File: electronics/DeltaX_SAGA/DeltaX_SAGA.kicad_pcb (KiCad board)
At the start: 4 copper layers, 50 x 50 mm, 73 parts, among them J1 USB_B_Micro, J10 M3_Encoder, J11 OUT-, J12 OUT+, J13 OUT-, J14 OUT+, J15 OUT-, J16 +, J17 -, J2 Programmer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

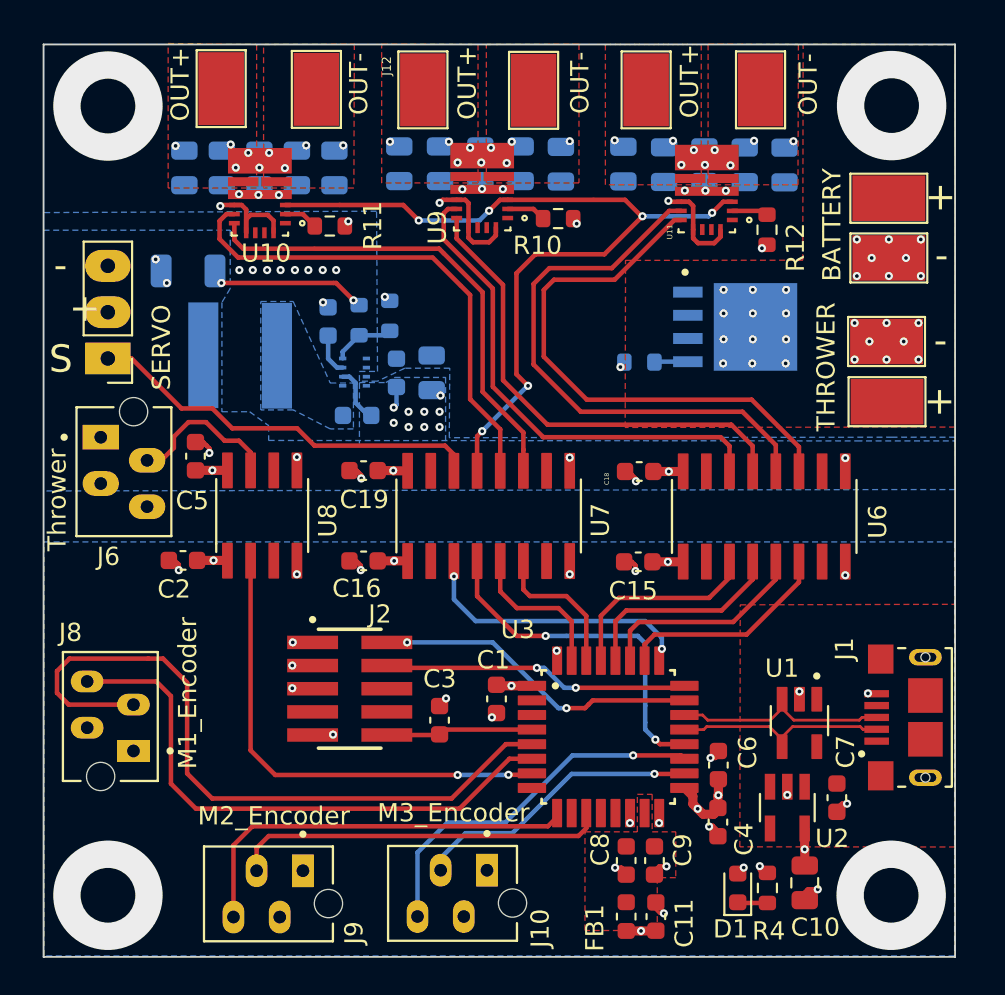
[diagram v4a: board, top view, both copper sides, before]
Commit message: PCB labels and routing optimised and updated
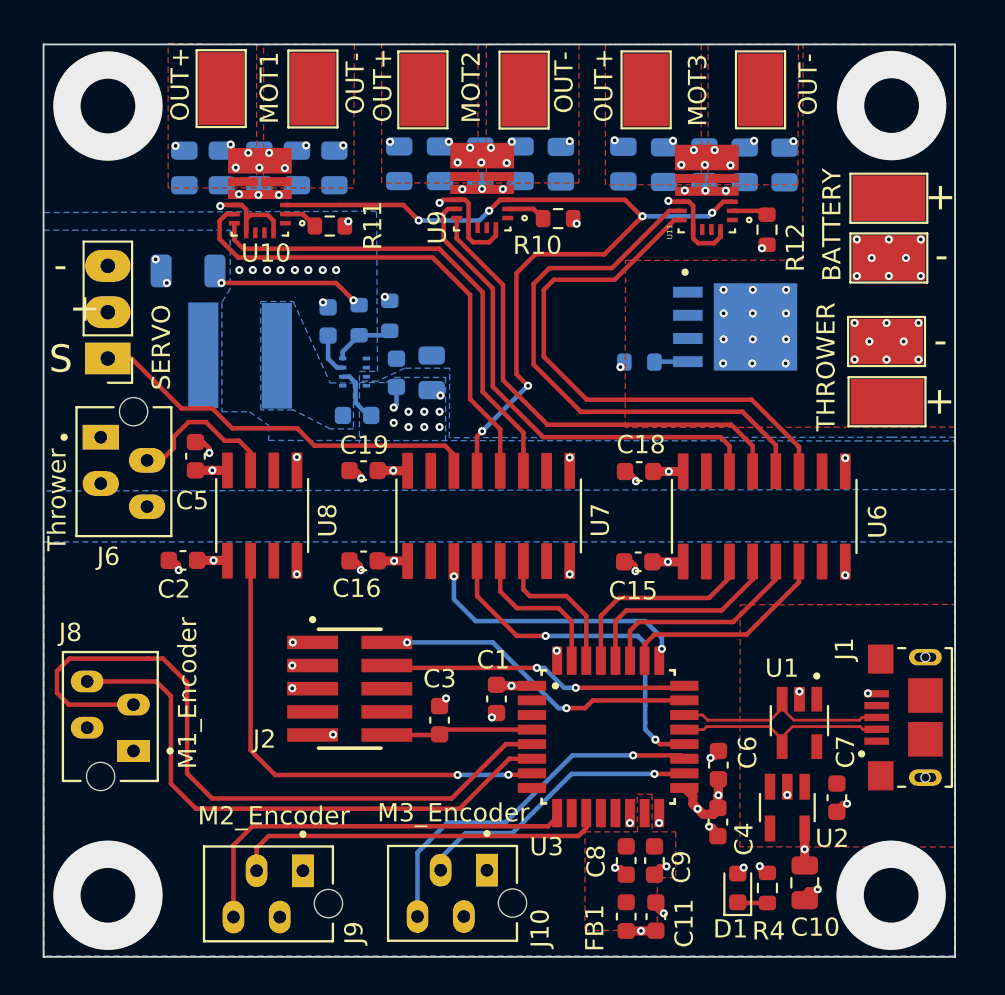
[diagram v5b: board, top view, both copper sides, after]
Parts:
- moved J13 0.52 mm to (152.3, 85.2)
- moved J11 0.19 mm to (140.7, 85.1)
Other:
- board text added: "MOT1"
- board text added: "MOT2"
- board text added: "MOT3"
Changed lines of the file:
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@@
     (property "Sheetname" "")
     (attr smd)
-    (fp_text reference "C8" (at -0.6026 1.4272 -270) (layer "F.SilkS")
+    (fp_text reference "C8" (at 0.0474 1.6472 -270) (layer "F.SilkS")
       (effects (font (size 1 1) (thickness 0.2)))
     )
@@
     (property "Sheetname" "")
     (attr through_hole)
-    (fp_text reference "J2" (at -4.0892 -1.6566) (layer "F.SilkS")
+    (fp_text reference "J2" (at 2.7708 4.6734) (layer "F.SilkS")
       (effects (font (size 1 1) (thickness 0.2)))
     )
@@
     (property "Sheetname" "")
     (attr through_hole)
-    (fp_text reference "U3" (at -4.9566 -5.8808) (layer "F.SilkS")
+    (fp_text reference "U3" (at -3.3766 6.0292) (layer "F.SilkS")
       (effects (font (size 1 1) (thickness 0.2)))
     )
@@
     (property "Sheetname" "")
     (attr smd)
-    (fp_text reference "J12" (at 1.2562 -1.9612 90 unlocked) (layer "F.SilkS")
+    (fp_text reference "J12" (at 1.2562 -1.9612 90 unlocked) (layer "F.Fab")
       (effects (font (size 0.5 0.5) (thickness 0.125)))
     )
-    (fp_text value "OUT+" (at 0.3362 2.4588 90 unlocked) (layer "F.SilkS")
+    (fp_text value "OUT+" (at 0.1962 -2.1712 90 unlocked) (layer "F.SilkS")
       (effects (font (size 1 1) (thickness 0.2)))
     )
@@
   )
   (footprint "1pinSMD:1PinSMD" (layer "F.Cu")
-    (at 152.8318 85.1916 90)
+    (at 152.31 85.18 90)
     (property "Sheetfile" "DeltaX_SAGA.kicad_sch")
     (property "Sheetname" "")
@@
       (effects (font (size 0.5 0.5) (thickness 0.125)))
     )
-    (fp_text value "OUT-" (at 0.3616 2.5682 90 unlocked) (layer "F.SilkS")
+    (fp_text value "OUT-" (at 0.37 2.22 90 unlocked) (layer "F.SilkS")
       (effects (font (size 1 1) (thickness 0.2)))
     )
@@
     (property "Sheetname" "")
     (attr smd)
-    (fp_text reference "C19" (at 0.0346 1.5942 180) (layer "F.SilkS")
+    (fp_text reference "C19" (at 0.0346 -1.3858 180) (layer "F.SilkS")
       (effects (font (size 1 1) (thickness 0.2)))
     )
@@
   )
   (footprint "1pinSMD:1PinSMD" (layer "F.Cu")
-    (at 140.9192 85.1408 90)
+    (at 140.73 85.12 90)
     (property "Sheetfile" "DeltaX_SAGA.kicad_sch")
     (property "Sheetname" "")
@@
     (property "Sheetname" "")
     (attr smd)
-    (fp_text reference "C18" (at -1.778 0.4064 90) (layer "F.SilkS")
-      (effects (font (size 0.25 0.25) (thickness 0.0625)))
+    (fp_text reference "C18" (at 0.1016 -1.4666 180) (layer "F.SilkS")
+      (effects (font (size 1 1) (thickness 0.2)))
     )
     (fp_text value "0.1uF" (at -0.7112 1.2446) (layer "F.Fab")
@@
       (effects (font (size 0.5 0.5) (thickness 0.125)))
     )
-    (fp_text value "OUT+" (at 0.4262 2.406 90 unlocked) (layer "F.SilkS")
+    (fp_text value "OUT+" (at 0.1962 -2.294 90 unlocked) (layer "F.SilkS")
       (effects (font (size 1 1) (thickness 0.2)))
     )
@@
     (property "Sheetname" "")
     (attr smd)
-    (fp_text reference "C9" (at -0.5726 -1.5434 90) (layer "F.SilkS")
+    (fp_text reference "C9" (at 0.3574 -1.4834 90) (layer "F.SilkS")
       (effects (font (size 1 1) (thickness 0.2)))
     )
@@
     (property "Sheetname" "")
     (attr through_hole)
-    (fp_text reference "Q1" (at -3.15355 -2.7664) (layer "B.SilkS")
-      (effects (font (size 1 1) (thickness 0.2)))
+    (fp_text reference "Q1" (at -3.15355 -2.7664 unlocked) (layer "B.SilkS")
+      (effects (font (size 1 1) (thickness 0.2)) (justify mirror))
     )
     (fp_text value "BUK6Y10" (at 0.3556 4.145 90) (layer "F.Fab")
@@
     (effects (font (size 1.5 1.5) (thickness 0.2)))
   )
+  (gr_text "MOT1" (at 138.37 85.11 90) (layer "F.SilkS")
+    (effects (font (size 1 1) (thickness 0.2)))
+  )
+  (gr_text "MOT2\n" (at 149.44 85.07 90) (layer "F.SilkS")
+    (effects (font (size 1 1) (thickness 0.2)))
+  )
   (gr_text "BATTERY" (at 169.22 92.62 90) (layer "F.SilkS")
     (effects (font (size 1 1) (thickness 0.2)))
@@
     (effects (font (size 1 1) (thickness 0.2)))
   )
+  (gr_text "MOT3" (at 161.86 85.24 90) (layer "F.SilkS")
+    (effects (font (size 1 1) (thickness 0.2)))
+  )
   (via (at 172.4914 86.0806) (size 6) (drill 3) (layers "F.Cu" "B.Cu") (free) (net 0))
   (via (at 129.5146 129.3876) (size 6) (drill 3) (layers "F.Cu" "B.Cu") (free) (net 0))
@@
   )
   (zone (net 4) (net_name "/V+") (layer "F.Cu") (hatch edge 0.508)
-    (connect_pads yes (clearance 0.1))
+    (connect_pads yes (clearance 0.25))
     (min_thickness 0.254) (filled_areas_thickness no)
     (fill yes (thermal_gap 0.508) (thermal_bridge_width 0.508))
@@
   (zone (net 82) (net_name "/VM") (layer "B.Cu") (hatch edge 0.508)
     (priority 2)
-    (connect_pads yes (clearance 0.005))
+    (connect_pads yes (clearance 0.25))
     (min_thickness 0.254) (filled_areas_thickness no)
     (fill yes (thermal_gap 0.508) (thermal_bridge_width 0.508))

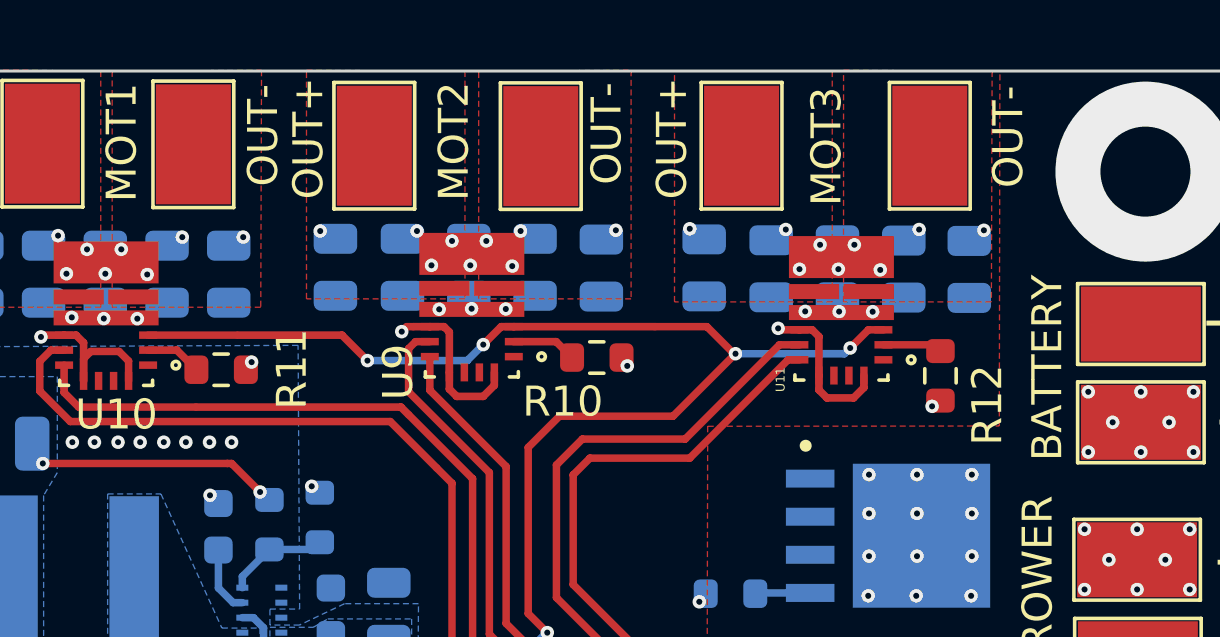
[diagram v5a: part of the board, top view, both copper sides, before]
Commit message: PCB design updated with labels aligned
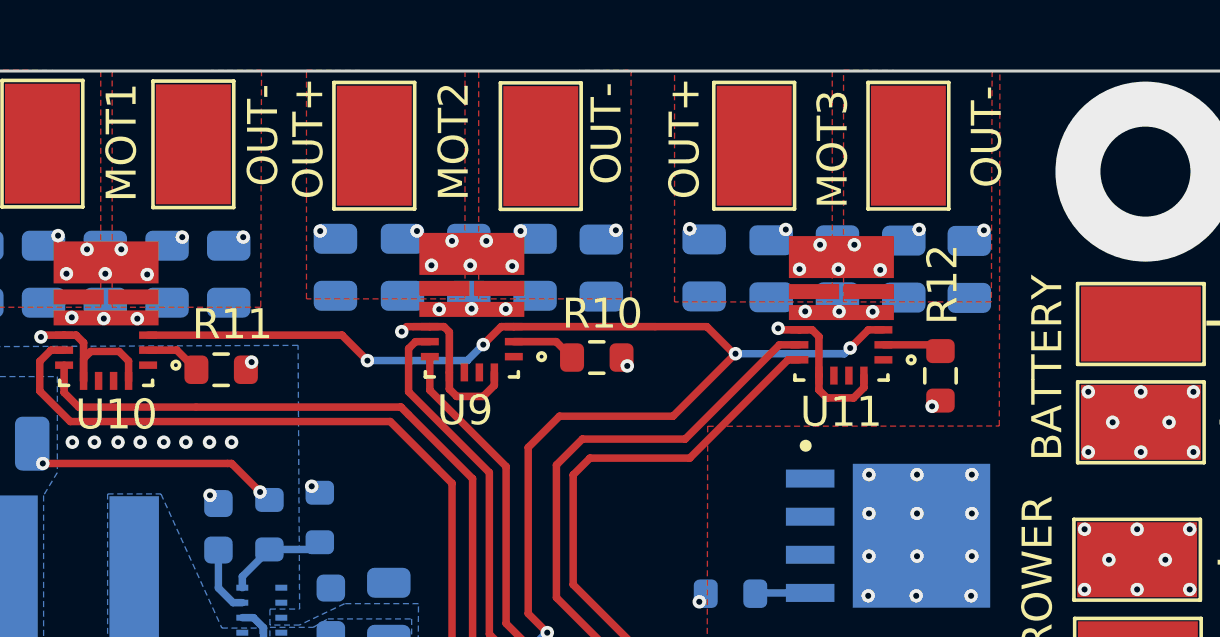
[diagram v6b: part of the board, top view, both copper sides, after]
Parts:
- moved J15 0.71 mm to (164.6, 85.2)
- moved J14 0.42 mm to (159.4, 85.2)
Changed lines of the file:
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@@
     (clearance 0.15)
     (attr smd)
-    (fp_text reference "U9" (at 2.4578 -2.136201 270) (layer "F.SilkS")
+    (fp_text reference "U9" (at 0.2278 -3.416201) (layer "F.SilkS")
       (effects (font (size 1 1) (thickness 0.2)))
     )
@@
     (property "Sheetname" "")
     (attr smd)
-    (fp_text reference "R11" (at -2.3588 0.0246 90) (layer "F.SilkS")
+    (fp_text reference "R11" (at -0.3788 1.5146 180) (layer "F.SilkS")
       (effects (font (size 1 1) (thickness 0.2)))
     )
@@
     (property "Sheetname" "")
     (attr smd)
-    (fp_text reference "R10" (at 1.1334 -1.4718 180) (layer "F.SilkS")
+    (fp_text reference "R10" (at -0.1866 1.4582 180) (layer "F.SilkS")
       (effects (font (size 1 1) (thickness 0.2)))
     )
@@
     (property "Sheetname" "")
     (attr smd)
-    (fp_text reference "R12" (at -0.9722 1.5612 270) (layer "F.SilkS")
+    (fp_text reference "R12" (at 3.0478 0.0712 270) (layer "F.SilkS")
       (effects (font (size 1 1) (thickness 0.2)))
     )
@@
   )
   (footprint "1pinSMD:1PinSMD" (layer "F.Cu")
-    (at 165.2778 85.1662 90)
+    (at 164.5646 85.1662 90)
     (property "Sheetfile" "DeltaX_SAGA.kicad_sch")
     (property "Sheetname" "")
@@
   )
   (footprint "1pinSMD:1PinSMD" (layer "F.Cu")
-    (at 159.004 85.1662 90)
+    (at 159.4246 85.1662 90)
     (property "Sheetfile" "DeltaX_SAGA.kicad_sch")
     (property "Sheetname" "")
@@
     (clearance 0.15)
     (attr smd)
-    (fp_text reference "U11" (at 2.0326 -2.2856 90) (layer "F.SilkS")
-      (effects (font (size 0.3 0.3) (thickness 0.075)))
+    (fp_text reference "U11" (at 0.0074 -3.3608 180) (layer "F.SilkS")
+      (effects (font (size 1 1) (thickness 0.2)))
     )
     (fp_text value "DRV8243" (at -0.0756 -3.1238 180) (layer "F.Fab")
@@
     (effects (font (size 1 1) (thickness 0.2)))
   )
-  (gr_text "MOT3" (at 161.86 85.24 90) (layer "F.SilkS")
+  (gr_text "MOT3" (at 162.07 85.33 90) (layer "F.SilkS")
     (effects (font (size 1 1) (thickness 0.2)))
   )

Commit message: PCB design updated
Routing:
- net /nSLEEP_Isolated: track 46.5 -> 47.5 mm
- net /VM: track 0.83 -> 0.00 mm

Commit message: PCB design updated
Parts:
- J11: value OUT- -> M12
- J12: value OUT+ -> M21
- J13: value OUT- -> M22
- J14: value OUT+ -> M31
- J15: value OUT- -> M33
- J4: value OUT+ -> M11
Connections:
- J10 pad 3: /Motor3_ENCA -> /Motor2_ENCA
- J10 pad 4: /Motor3_ENCB -> /Motor2_ENCB
- J9 pad 3: /Motor2_ENCA -> /Motor3_ENCA
- J9 pad 4: /Motor2_ENCB -> /Motor3_ENCB
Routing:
- net /Motor3_PWM_Isolated: track 30.7 -> 18.8 mm
- net /Motor3_DIR_Isolated: track 30.2 -> 19.5 mm
- net /Motor2_ENCA: track 20.6 -> 10.0 mm
- net /Motor3_ENCA: track 16.0 -> 26.4 mm, vias 1 -> 2
- net /Motor3_ENCB: track 20.4 -> 30.7 mm, vias 1 -> 2
- net /Motor2_ENCB: track 22.5 -> 12.3 mm
- net /SWCLK: track 16.9 -> 24.5 mm
- net /SWDIO: track 18.0 -> 21.3 mm
- net /Motor1_ENCB: track 31.2 -> 27.9 mm
- net /Thrower_PWM: track 26.4 -> 29.3 mm
- net /Servo_PWM: track 15.7 -> 17.8 mm
- net /nSLEEP_Isolated: track 47.5 -> 49.5 mm
- net /Motor1_PWM_Isolated: track 27.3 -> 26.0 mm
- net /Motor1_DIR_Isolated: track 26.4 -> 25.6 mm
- net /nSLEEP: track 19.4 -> 18.7 mm
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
